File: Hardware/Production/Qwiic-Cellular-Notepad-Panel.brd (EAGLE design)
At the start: 151.9 x 161.3 mm, 714 parts, among them J10 U.FL, J12 U.FL, J14 I2C, J15 SIM Socket, J17 QWIIC_RIGHT_ANGLE, J18 I2C, J23 External SIM, J24 QWIIC_RIGHT_ANGLE, J25 U.FL, J26 U.FL, J27 SIM Socket, J3 QWIIC_RIGHT_ANGLE, J32 QWIIC_RIGHT_ANGLE, J33 I2C, J38 External SIM, J39 QWIIC_RIGHT_ANGLE, J40 U.FL, J41 U.FL, J42 SIM Socket, J47 QWIIC_RIGHT_ANGLE, J48 I2C, J53 External SIM, J54 QWIIC_RIGHT_ANGLE, J55 U.FL, J56 U.FL, J57 SIM Socket, J6 External SIM, J62 QWIIC_RIGHT_ANGLE, J63 I2C, J68 External SIM, J69 QWIIC_RIGHT_ANGLE, J70 U.FL, J71 U.FL, J72 SIM Socket, J77 QWIIC_RIGHT_ANGLE, J78 I2C, J8 QWIIC_RIGHT_ANGLE, J83 External SIM, J84 QWIIC_RIGHT_ANGLE, J85 U.FL, J86 U.FL, J87 SIM Socket, U1 MCP73831, U10 BLUES NOTECARD, U11 MCP73831, U12 BLUES NOTECARD, U2 MCP73831, U3 BLUES NOTECARD, U4 BLUES NOTECARD, U5 MCP73831, U6 BLUES NOTECARD, U7 MCP73831, U8 BLUES NOTECARD, U9 MCP73831

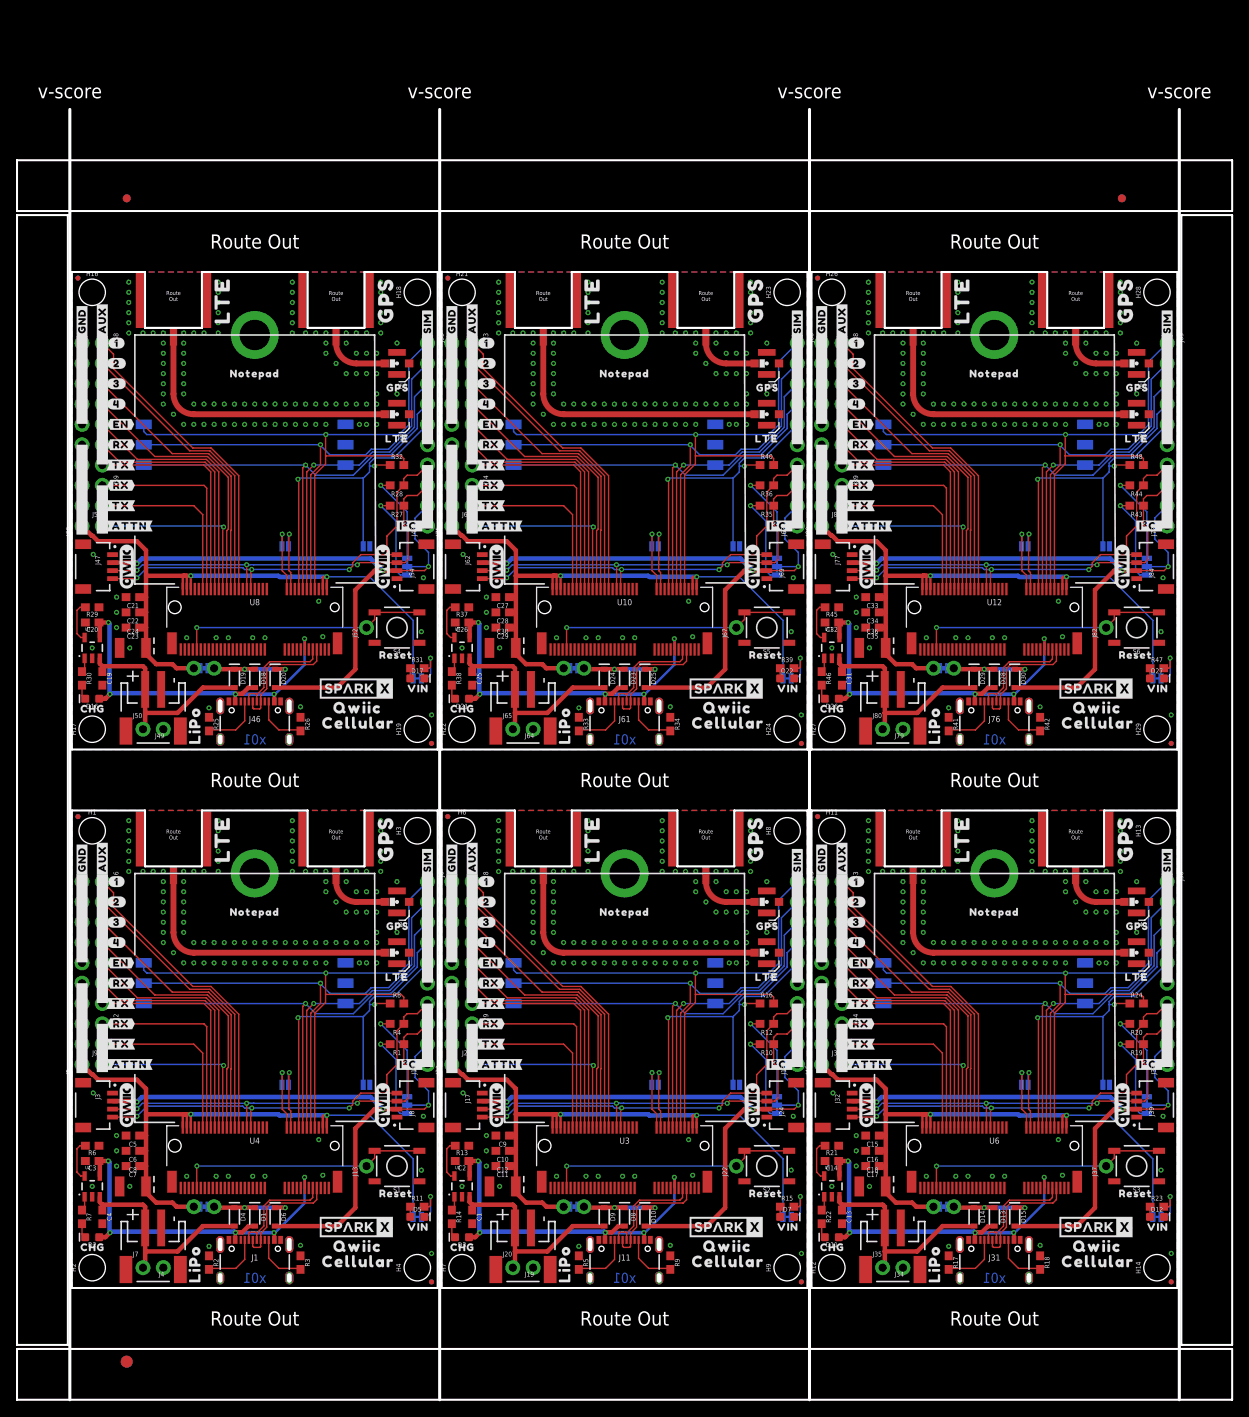
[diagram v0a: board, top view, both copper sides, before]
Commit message: Fix Notecard FP. Add VIO vreg. x02 release.
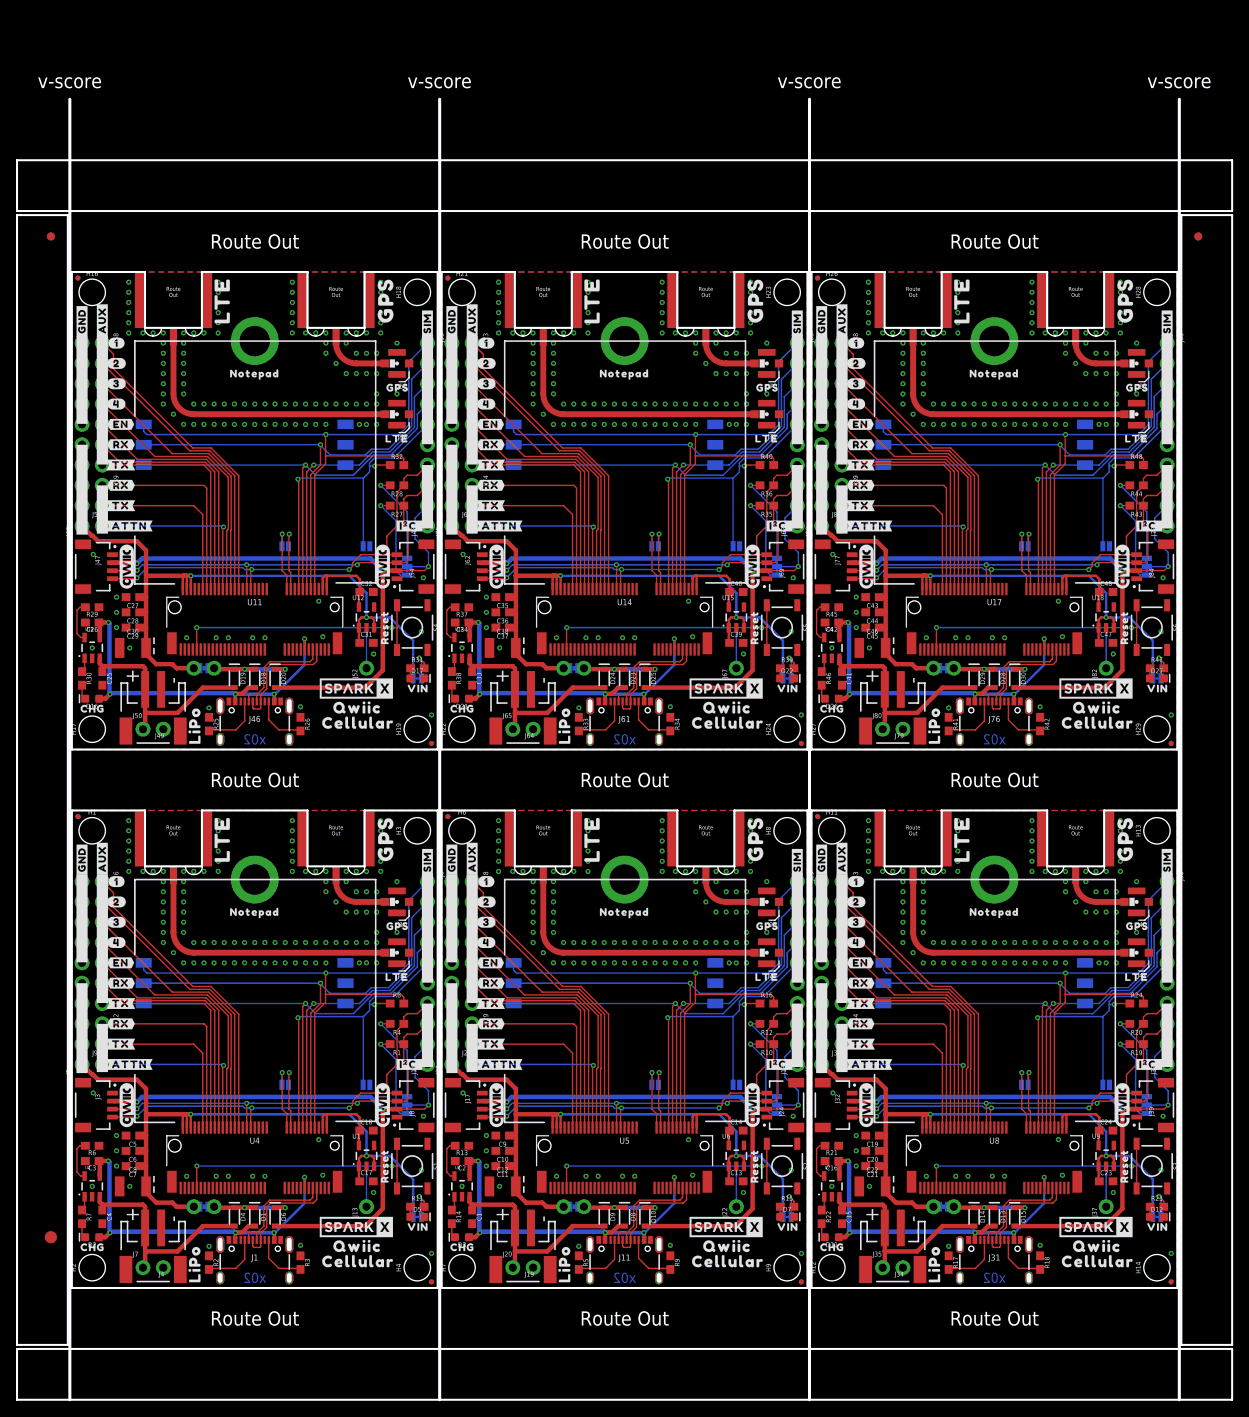
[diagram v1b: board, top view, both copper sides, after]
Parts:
- added C37, C45: 0.22uF, SparkFun-Capacitors:0603
- added C38, C46: 68uF, SparkFun-Capacitors:EIA3528
- added C39, C40, C43, C47, C48: 1.0uF, SparkFun-Capacitors:0603
- added C41, C42: 4.7uF, SparkFun-Capacitors:0603
- added C44: 0.1uF, SparkFun-Capacitors:0603
- added U13, U16: MCP73831, SparkFun-IC-Power:SOT23-5
- added U14, U17: BLUES NOTECARD, Notecard:M.2-CONNECTOR-E
- added U15, U18: STLQ015-3.3V, SparkFun-IC-Power:SOT23-5
- C13, C14, C19, C31, C32: value 4.7uF -> 1.0uF
- C15, C33: value 1.0uF -> 4.7uF
- C16, C34: value 0.1uF -> 4.7uF
- C17, C23, C35: value 0.22uF -> 1.0uF
- C18, C24: value 68uF -> 1.0uF; device SparkFun-Capacitors:EIA3528 -> SparkFun-Capacitors:0603
- C20: value 4.7uF -> 0.1uF
- C21: value 1.0uF -> 0.22uF
- C22: value 0.1uF -> 68uF; device SparkFun-Capacitors:0603 -> SparkFun-Capacitors:EIA3528
- C36: value 68uF -> 0.1uF; device SparkFun-Capacitors:EIA3528 -> SparkFun-Capacitors:0603
- E1, E10, E11, E12, E2, E3, E4, E5, E6, E7, E8, E9: value (none) -> SMA
- H10, H15, H20, H25, H30, H5: value STAND-OFF-REFLOW2.5MM_TALL -> STAND-OFF
- U1, U9: value MCP73831 -> STLQ015-3.3V
- U10, U3: value BLUES NOTECARD -> MCP73831; device Notecard:M.2-CONNECTOR-E -> SparkFun-IC-Power:SOT23-5
- U11, U5: value MCP73831 -> BLUES NOTECARD; device SparkFun-IC-Power:SOT23-5 -> Notecard:M.2-CONNECTOR-E
- U12, U6: value BLUES NOTECARD -> STLQ015-3.3V; device Notecard:M.2-CONNECTOR-E -> SparkFun-IC-Power:SOT23-5
- moved C23 140.0 mm to (129.3, 13.3), turned to 0 degrees
- moved C24 135.8 mm to (129.3, 19.7)
- moved C20 117.8 mm to (100.1, 17.1)
- moved C22 117.0 mm to (100.1, 12.7), turned to 0 degrees
- moved C21 116.6 mm to (100.1, 15.2)
- moved U8 114.4 mm to (115.3, 17.8)
- moved U7 114.4 mm to (95.0, 12.7)
- moved C19 112.0 mm to (100.1, 19.1), turned to 180 degrees
- moved U9 102.5 mm to (129.3, 16.5)
- moved U12 78.5 mm to (36.8, 83.8)
- moved U11 72.3 mm to (22.9, 85.1)
- moved U10 66.7 mm to (2.54, 80.0)
- moved E2 66.5 mm to (79.2, 59.7)
- moved E3 66.5 mm to (12.7, 59.7)
- moved C18 63.6 mm to (36.8, 19.7)
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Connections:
- new net VIO: C18.1, U1.5, U4.2, U4.4
- new net VIO1: C14.1, U5.2, U5.4, U6.5
- new net VIO2: C24.1, U8.2, U8.4, U9.5
- new net VIO3: C32.1, U11.2, U11.4, U12.5
- new net VIO4: C40.1, U14.2, U14.4, U15.5
- new net VIO5: C48.1, U17.2, U17.4, U18.5
- net !RESET!1: now also U5.67; no longer U3.67
- net !RESET!2: now also U8.67; no longer U6.67
- net !RESET!3: now also U11.67; no longer U8.67
- net !RESET!4: now also U14.67; no longer U10.67
- net !RESET!5: now also U17.67; no longer U12.67
- net ATTN1: now also U5.54; no longer U3.54
- net ATTN2: now also U8.54; no longer U6.54
- net ATTN3: now also U11.54; no longer U8.54
- net ATTN4: now also U14.54; no longer U10.54
- net ATTN5: now also U17.54; no longer U12.54
- net AUX10: now also U8.48; no longer U6.48
- net AUX11: now also U8.50; no longer U6.50
- net AUX12: now also U8.52; no longer U6.52
- net AUX13: now also U11.46; no longer U8.46
- net AUX14: now also U11.48; no longer U8.48
- net AUX15: now also U11.50; no longer U8.50
- net AUX16: now also U11.52; no longer U8.52
- net AUX17: now also U14.46; no longer U10.46
- net AUX18: now also U14.48; no longer U10.48
- net AUX19: now also U14.50; no longer U10.50
- net AUX20: now also U14.52; no longer U10.52
- net AUX21: now also U17.46; no longer U12.46
- net AUX22: now also U17.48; no longer U12.48
- net AUX23: now also U17.50; no longer U12.50
- net AUX24: now also U17.52; no longer U12.52
- net AUX5: now also U5.46; no longer U3.46
- net AUX6: now also U5.48; no longer U3.48
- net AUX7: now also U5.50; no longer U3.50
- net AUX8: now also U5.52; no longer U3.52
- net AUX9: now also U8.46; no longer U6.46
- net AUX_EN1: now also U5.56; no longer U3.56
- net AUX_EN2: now also U8.56; no longer U6.56
- net AUX_EN3: now also U11.56; no longer U8.56
- net AUX_EN4: now also U14.56; no longer U10.56
- net AUX_EN5: now also U17.56; no longer U12.56
- net AUX_RX1: now also U5.58; no longer U3.58
- net AUX_RX2: now also U8.58; no longer U6.58
- net AUX_RX3: now also U11.58; no longer U8.58
- net AUX_RX4: now also U14.58; no longer U10.58
- net AUX_RX5: now also U17.58; no longer U12.58
- net AUX_TX1: now also U5.60; no longer U3.60
- net AUX_TX2: now also U8.60; no longer U6.60
- net AUX_TX3: now also U11.60; no longer U8.60
- net AUX_TX4: now also U14.60; no longer U10.60
- net AUX_TX5: now also U17.60; no longer U12.60
- net CHG_LED1: now also U3.1; no longer U1.1
- net CHG_LED2: now also U7.1; no longer U5.1
- net CHG_LED3: now also U10.1; no longer U7.1
- net CHG_LED4: now also U13.1; no longer U9.1
- net CHG_LED5: now also U16.1; no longer U11.1
- net GND: now also C17.2, C18.2, E3.GND@0, E3.GND@1, E4.GND@0, E4.GND@1, U1.2; no longer E1.GND@0, E1.GND@1, E2.GND@0, E2.GND@1
- net GND1: now also C13.2, C14.2, E1.GND@0, E1.GND@1, E2.GND@0, E2.GND@1, U3.2, U5.11, U5.18, U5.3, U5.33, U5.39, U5.45, U5.5, U5.51, U5.57, U5.6, U5.71, U5.73, U6.2; no longer E3.GND@0, E3.GND@1, E4.GND@0, E4.GND@1, U1.2, U3.11, U3.18, U3.3, U3.33, U3.39, U3.45, U3.5, U3.51, U3.57, U3.6, U3.71, U3.73
- net GND2: now also C19.2, C20.2, C21.2, C22.C, C23.2, C24.2, U7.2, U8.11, U8.18, U8.3, U8.33, U8.39, U8.45, U8.5, U8.51, U8.57, U8.6, U8.71, U8.73, U9.2; no longer C13.2, C14.2, C17.2, C18.C, U5.2, U6.11, U6.18, U6.3, U6.33, U6.39, U6.45, U6.5, U6.51, U6.57, U6.6, U6.71, U6.73
- net GND3: now also C25.2, C26.2, C27.2, C28.2, C29.2, C30.C, C31.2, C32.2, U10.2, U11.11, U11.18, U11.3, U11.33, U11.39, U11.45, U11.5, U11.51, U11.57, U11.6, U11.71, U11.73, U12.2; no longer C19.2, C20.2, C21.2, C22.2, C23.2, C24.C, U7.2, U8.11, U8.18, U8.3, U8.33, U8.39, U8.45, U8.5, U8.51, U8.57, U8.6, U8.71, U8.73
- net GND4: now also C33.2, C34.2, C35.2, C36.2, C37.2, C38.C, C39.2, C40.2, U13.2, U14.11, U14.18, U14.3, U14.33, U14.39, U14.45, U14.5, U14.51, U14.57, U14.6, U14.71, U14.73, U15.2; no longer C25.2, C26.2, C27.2, C28.2, C29.2, C30.C, U10.11, U10.18, U10.3, U10.33, U10.39, U10.45, U10.5, U10.51, U10.57, U10.6, U10.71, U10.73, U9.2
- net GND5: now also C41.2, C42.2, C43.2, C44.2, C45.2, C46.C, C47.2, C48.2, U16.2, U17.11, U17.18, U17.3, U17.33, U17.39, U17.45, U17.5, U17.51, U17.57, U17.6, U17.71, U17.73, U18.2; no longer C31.2, C32.2, C33.2, C34.2, C35.2, C36.C, U11.2, U12.11, U12.18, U12.3, U12.33, U12.39, U12.45, U12.5, U12.51, U12.57, U12.6, U12.71, U12.73
- net N$13: now also U3.5; no longer U1.5
- net N$21: now also U7.5; no longer U5.5
- net N$29: now also U10.5; no longer U7.5
- net N$37: now also U13.5; no longer U9.5
- net N$45: now also U16.5; no longer U11.5
- net RF_GPS: now also E4.SIG; no longer E1.SIG
- net RF_GPS1: now also E2.SIG; no longer E3.SIG
- net RF_GPS2: now also E6.SIG; no longer E5.SIG
- net RF_GPS3: now also E8.SIG; no longer E7.SIG
- net RF_GPS4: now also E10.SIG; no longer E9.SIG
- net RF_GPS5: now also E12.SIG; no longer E11.SIG
- net RF_LTE: now also E3.SIG; no longer E2.SIG
- net RF_LTE1: now also E1.SIG; no longer E4.SIG
- net RF_LTE2: now also E5.SIG; no longer E6.SIG
- net RF_LTE3: now also E7.SIG; no longer E8.SIG
- net RF_LTE4: now also E9.SIG; no longer E10.SIG
- net RF_LTE5: now also E11.SIG; no longer E12.SIG
- net RX1: now also U5.62; no longer U3.62
- net RX2: now also U8.62; no longer U6.62
- net RX3: now also U11.62; no longer U8.62
- net RX4: now also U14.62; no longer U10.62
- net RX5: now also U17.62; no longer U12.62
- net SCL1: now also U5.40; no longer U3.40
- net SCL2: now also U8.40; no longer U6.40
- net SCL3: now also U11.40; no longer U8.40
- net SCL4: now also U14.40; no longer U10.40
- net SCL5: now also U17.40; no longer U12.40
- net SDA1: now also U5.42; no longer U3.42
- net SDA2: now also U8.42; no longer U6.42
- net SDA3: now also U11.42; no longer U8.42
- net SDA4: now also U14.42; no longer U10.42
- net SDA5: now also U17.42; no longer U12.42
- net SIM_!CD!1: now also U5.16; no longer U3.16
- net SIM_!CD!2: now also U8.16; no longer U6.16
- net SIM_!CD!3: now also U11.16; no longer U8.16
- net SIM_!CD!4: now also U14.16; no longer U10.16
- net SIM_!CD!5: now also U17.16; no longer U12.16
- net SIM_CLK1: now also U5.14; no longer U3.14
- net SIM_CLK2: now also U8.14; no longer U6.14
- net SIM_CLK3: now also U11.14; no longer U8.14
- net SIM_CLK4: now also U14.14; no longer U10.14
- net SIM_CLK5: now also U17.14; no longer U12.14
- net SIM_IO1: now also U5.12; no longer U3.12
- net SIM_IO2: now also U8.12; no longer U6.12
- net SIM_IO3: now also U11.12; no longer U8.12
- net SIM_IO4: now also U14.12; no longer U10.12
- net SIM_IO5: now also U17.12; no longer U12.12
- net SIM_RST1: now also U5.10; no longer U3.10
- net SIM_RST2: now also U8.10; no longer U6.10
- net SIM_RST3: now also U11.10; no longer U8.10
- net SIM_RST4: now also U14.10; no longer U10.10
- net SIM_RST5: now also U17.10; no longer U12.10
- net SIM_VCC1: now also U5.8; no longer U3.8
- net SIM_VCC2: now also U8.8; no longer U6.8
- net SIM_VCC3: now also U11.8; no longer U8.8
- net SIM_VCC4: now also U14.8; no longer U10.8
- net SIM_VCC5: now also U17.8; no longer U12.8
- net TX1: now also U5.64; no longer U3.64
- net TX2: now also U8.64; no longer U6.64
- net TX3: now also U11.64; no longer U8.64
- net TX4: now also U14.64; no longer U10.64
- net TX5: now also U17.64; no longer U12.64
- net USB_D+1: now also U5.7; no longer U3.7
- net USB_D+2: now also U8.7; no longer U6.7
- net USB_D+3: now also U11.7; no longer U8.7
- net USB_D+4: now also U14.7; no longer U10.7
- net USB_D+5: now also U17.7; no longer U12.7
- net USB_D-1: now also U5.9; no longer U3.9
- net USB_D-2: now also U8.9; no longer U6.9
- net USB_D-3: now also U11.9; no longer U8.9
- net USB_D-4: now also U14.9; no longer U10.9
- net USB_D-5: now also U17.9; no longer U12.9
- net VACT_GPS_IN1: now also U5.22; no longer U3.22
- net VACT_GPS_IN2: now also U8.22; no longer U6.22
- net VACT_GPS_IN3: now also U11.22; no longer U8.22
- net VACT_GPS_IN4: now also U14.22; no longer U10.22
- net VACT_GPS_IN5: now also U17.22; no longer U12.22
- net VACT_GPS_OUT1: now also U5.20; no longer U3.20
- net VACT_GPS_OUT2: now also U8.20; no longer U6.20
- net VACT_GPS_OUT3: now also U11.20; no longer U8.20
- net VACT_GPS_OUT4: now also U14.20; no longer U10.20
- net VACT_GPS_OUT5: now also U17.20; no longer U12.20
- net VIN: now also C17.1, U1.1, U1.3; no longer U4.2, U4.4
- net VIN10: now also C43.1, C44.1, C45.1, C46.A, C47.1, U17.70, U17.72, U17.74, U18.1, U18.3; no longer C33.1, C34.1, C35.1, C36.A, U12.2, U12.4, U12.70, U12.72, U12.74
- net VIN2: now also C13.1, U5.70, U5.72, U5.74, U6.1, U6.3; no longer U3.2, U3.4, U3.70, U3.72, U3.74
- net VIN4: now also C19.1, C20.1, C21.1, C22.A, C23.1, U8.70, U8.72, U8.74, U9.1, U9.3; no longer C15.1, C16.1, C17.1, C18.A, U6.2, U6.4, U6.70, U6.72, U6.74
- net VIN6: now also C27.1, C28.1, C29.1, C30.A, C31.1, U11.70, U11.72, U11.74, U12.1, U12.3; no longer C21.1, C22.1, C23.1, C24.A, U8.2, U8.4, U8.70, U8.72, U8.74
- net VIN8: now also C35.1, C36.1, C37.1, C38.A, C39.1, U14.70, U14.72, U14.74, U15.1, U15.3; no longer C27.1, C28.1, C29.1, C30.A, U10.2, U10.4, U10.70, U10.72, U10.74
- net V_BATT1: now also U3.3; no longer U1.3
- net V_BATT2: now also C15.1, U7.3; no longer C13.1, U5.3
- net V_BATT3: now also C25.1, U10.3; no longer C19.1, U7.3
- net V_BATT4: now also C33.1, U13.3; no longer C25.1, U9.3
- net V_BATT5: now also C41.1, U16.3; no longer C31.1, U11.3
- net V_USB1: now also U3.4, U5.13; no longer U1.4, U3.13
- net V_USB2: now also C16.1, U7.4, U8.13; no longer C14.1, U5.4, U6.13
- net V_USB3: now also C26.1, U10.4, U11.13; no longer C20.1, U7.4, U8.13
- net V_USB4: now also C34.1, U13.4, U14.13; no longer C26.1, U10.13, U9.4
- net V_USB5: now also C42.1, U16.4, U17.13; no longer C32.1, U11.4, U12.13
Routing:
- net VIO4: track 0.00 -> 11.5 mm
- net VIO5: track 0.00 -> 11.5 mm
- net VIO3: track 0.00 -> 11.5 mm
- net VIO1: track 0.00 -> 11.5 mm
- net VIO2: track 0.00 -> 11.5 mm
- net VIO: track 0.00 -> 11.5 mm
- net !RESET!2: track 31.9 -> 38.4 mm, vias 1 -> 2
- net !RESET!5: track 31.9 -> 38.4 mm, vias 1 -> 2
- net !RESET!: track 31.9 -> 38.4 mm, vias 1 -> 2
- net !RESET!3: track 31.9 -> 38.4 mm, vias 1 -> 2
- net !RESET!1: track 31.9 -> 38.4 mm, vias 1 -> 2
- net !RESET!4: track 31.9 -> 38.4 mm, vias 1 -> 2
- net VIN: track 94.1 -> 97.0 mm
- net VIN4: track 94.1 -> 97.0 mm
- net VIN6: track 94.1 -> 97.0 mm
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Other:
- board size 151.9 x 161.3 mm -> 151.9 x 162.6 mm
- board text added: "x02"
- board text removed: "x01"

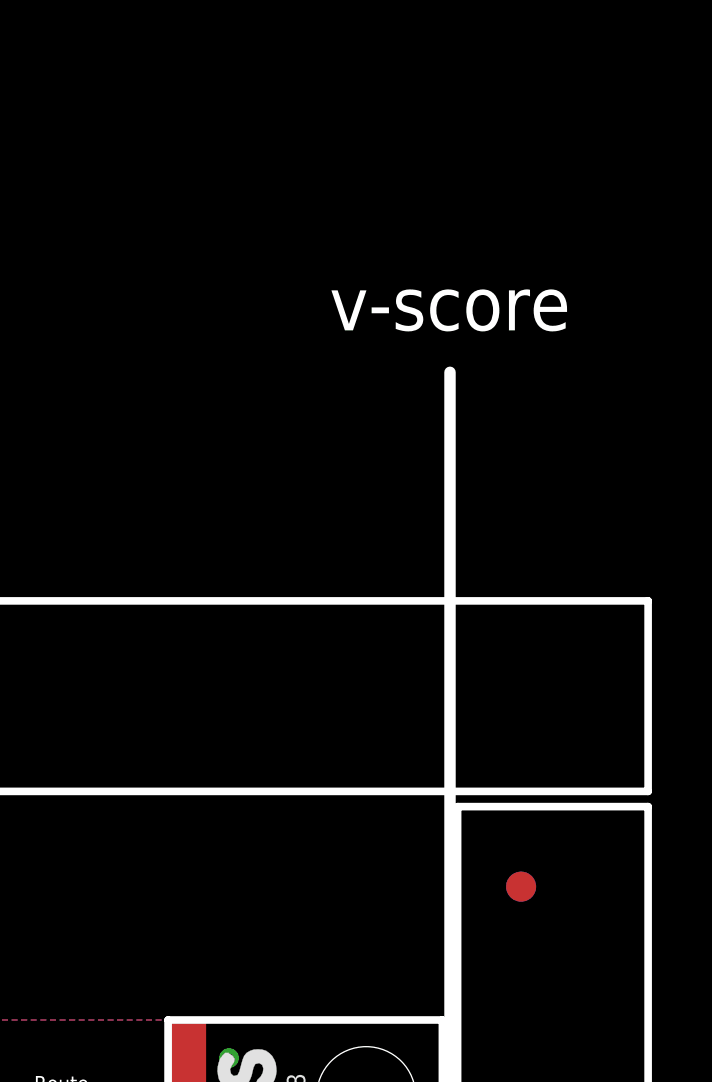
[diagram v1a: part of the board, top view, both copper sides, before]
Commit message: Change to 22uF cap. Add production files.
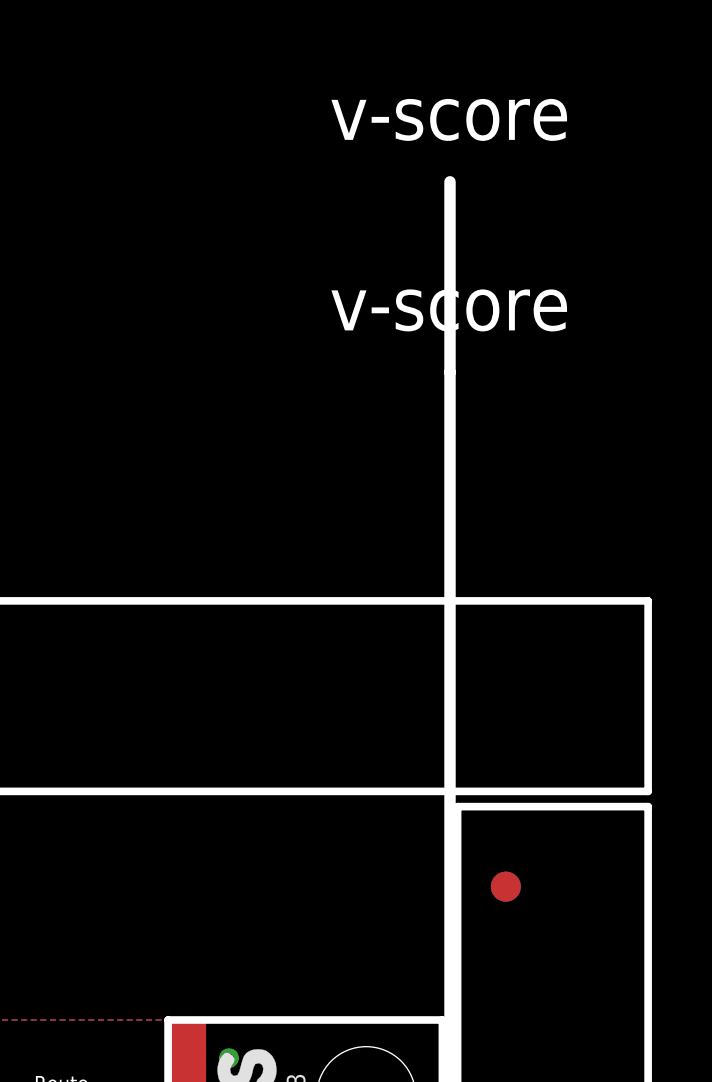
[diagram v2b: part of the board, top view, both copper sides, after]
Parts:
- moved E$3 0.51 mm to (140.3, 131.4)
- moved E$4 0.51 mm to (140.3, 131.4)
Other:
- board size 151.9 x 162.6 mm -> 151.9 x 168.9 mm
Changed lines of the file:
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@@
 <wire x1="138.43" y1="-13.97" x2="138.43" y2="148.59" width="0.381" layer="46"/>
 <text x="138.43" y="150.876" size="1.778" layer="46" font="vector" ratio="15" align="center">v-score</text>
+<wire x1="138.43" y1="148.59" x2="138.43" y2="154.94" width="0.381" layer="46"/>
+<text x="138.43" y="157.226" size="1.778" layer="46" font="vector" ratio="15" align="center">v-score</text>
 <wire x1="-6.858" y1="-7.62" x2="145.034" y2="-7.62" width="0.254" layer="20"/>
 <wire x1="145.034" y1="-7.62" x2="145.034" y2="-13.97" width="0.254" layer="20"/>
@@
 <element name="E$1" library="SparkFun-Aesthetics" package="FIDUCIAL-1X2" value="" x="-2.62381875" y="131.445" smashed="yes"/>
 <element name="E$2" library="SparkFun-Aesthetics" package="FIDUCIAL-1X2" value="" x="-2.62381875" y="131.445" smashed="yes" rot="MR0"/>
-<element name="E$3" library="SparkFun-Aesthetics" package="FIDUCIAL-1X2" value="" x="140.79981875" y="131.445" smashed="yes"/>
-<element name="E$4" library="SparkFun-Aesthetics" package="FIDUCIAL-1X2" value="" x="140.79981875" y="131.445" smashed="yes" rot="MR0"/>
+<element name="E$3" library="SparkFun-Aesthetics" package="FIDUCIAL-1X2" value="" x="140.29181875" y="131.445" smashed="yes"/>
+<element name="E$4" library="SparkFun-Aesthetics" package="FIDUCIAL-1X2" value="" x="140.29181875" y="131.445" smashed="yes" rot="MR0"/>
 <element name="E$5" library="SparkFun-Retired" package="FIDUCIAL-1.5X3" value="" x="-2.62381875" y="6.35" smashed="yes"/>
 <element name="E$6" library="SparkFun-Retired" package="FIDUCIAL-1.5X3" value="" x="-2.62381875" y="6.35" smashed="yes" rot="MR0"/>
